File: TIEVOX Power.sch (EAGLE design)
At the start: 15 parts, among them IC1 NE555P, T1 2N222A

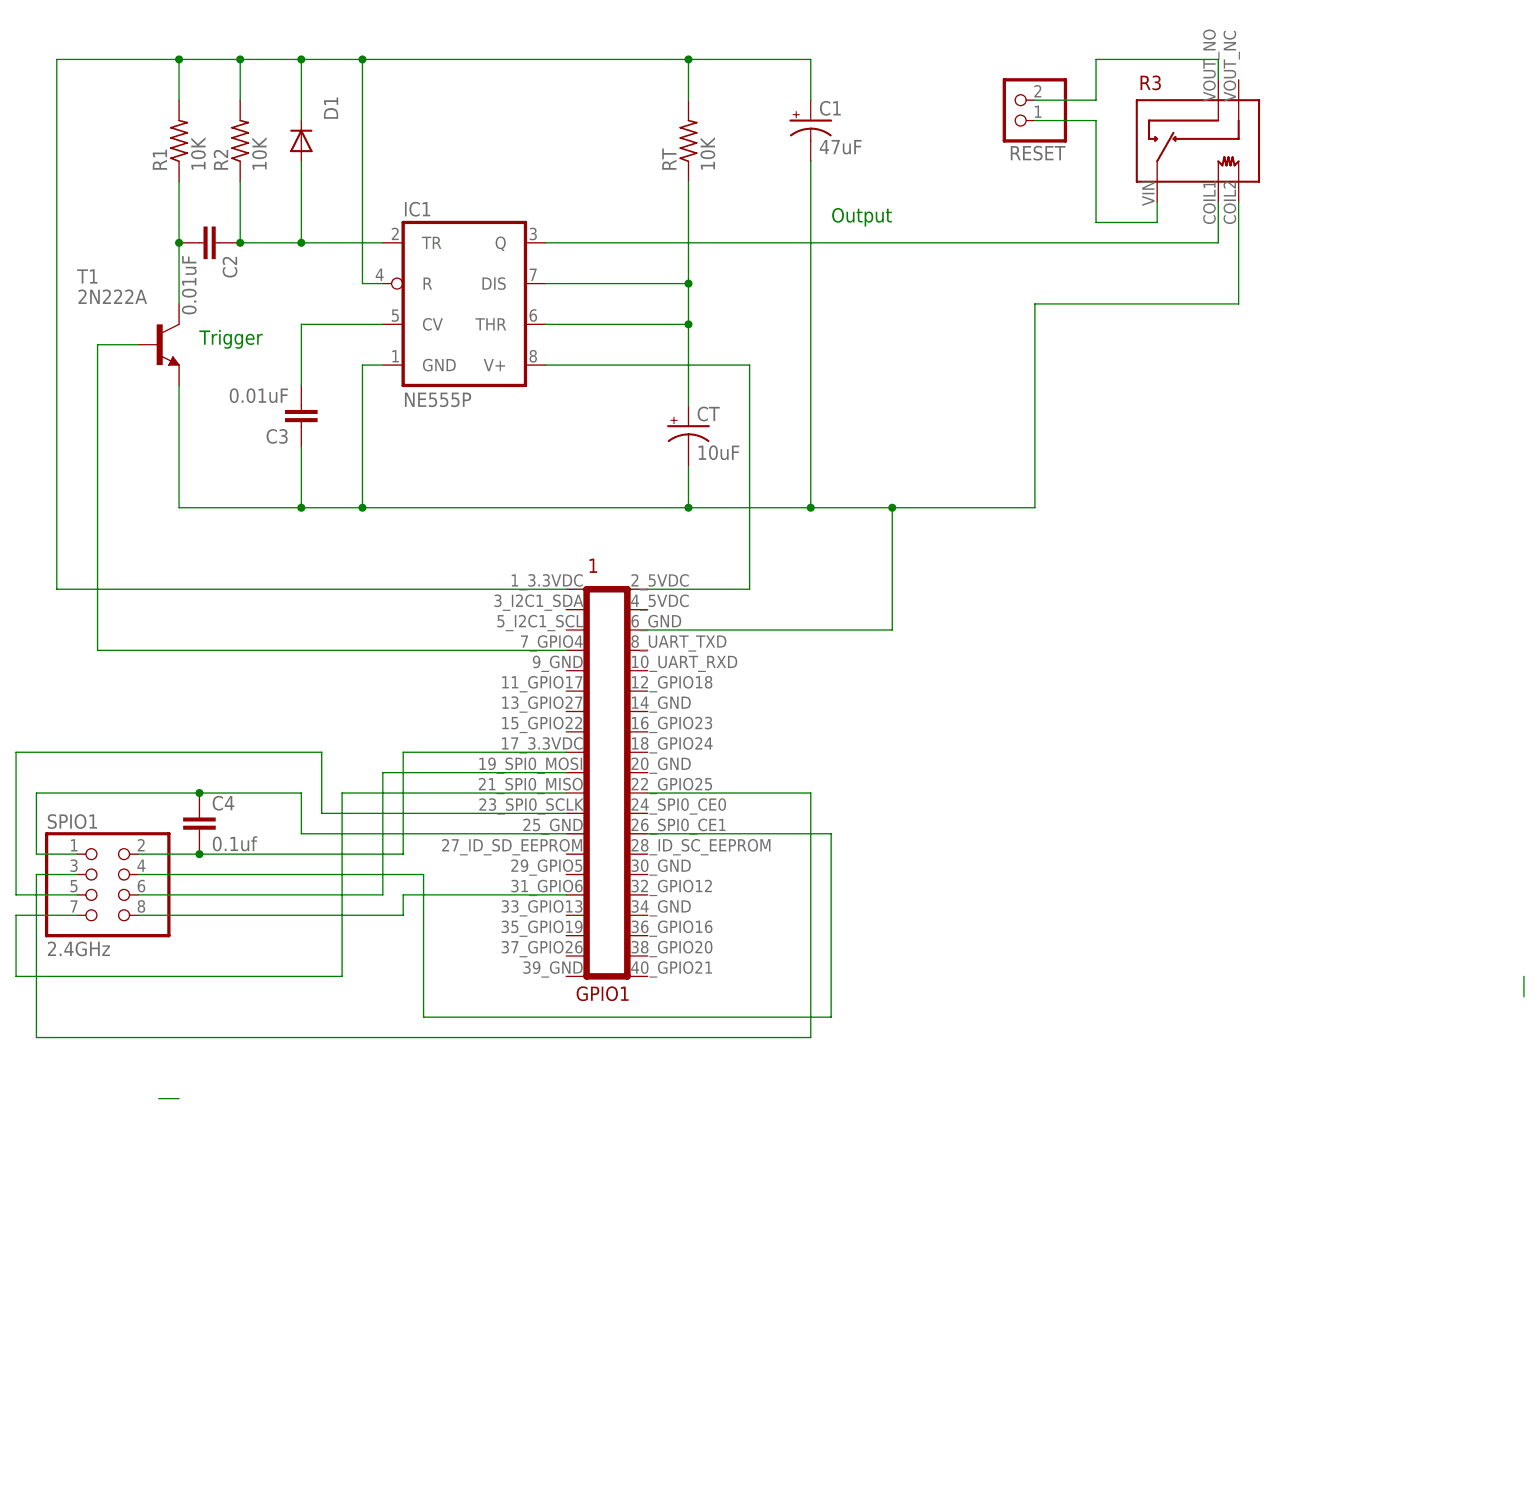
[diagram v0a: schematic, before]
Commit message: Should have working versions of all required boards now.
Updated to No Commercial license.
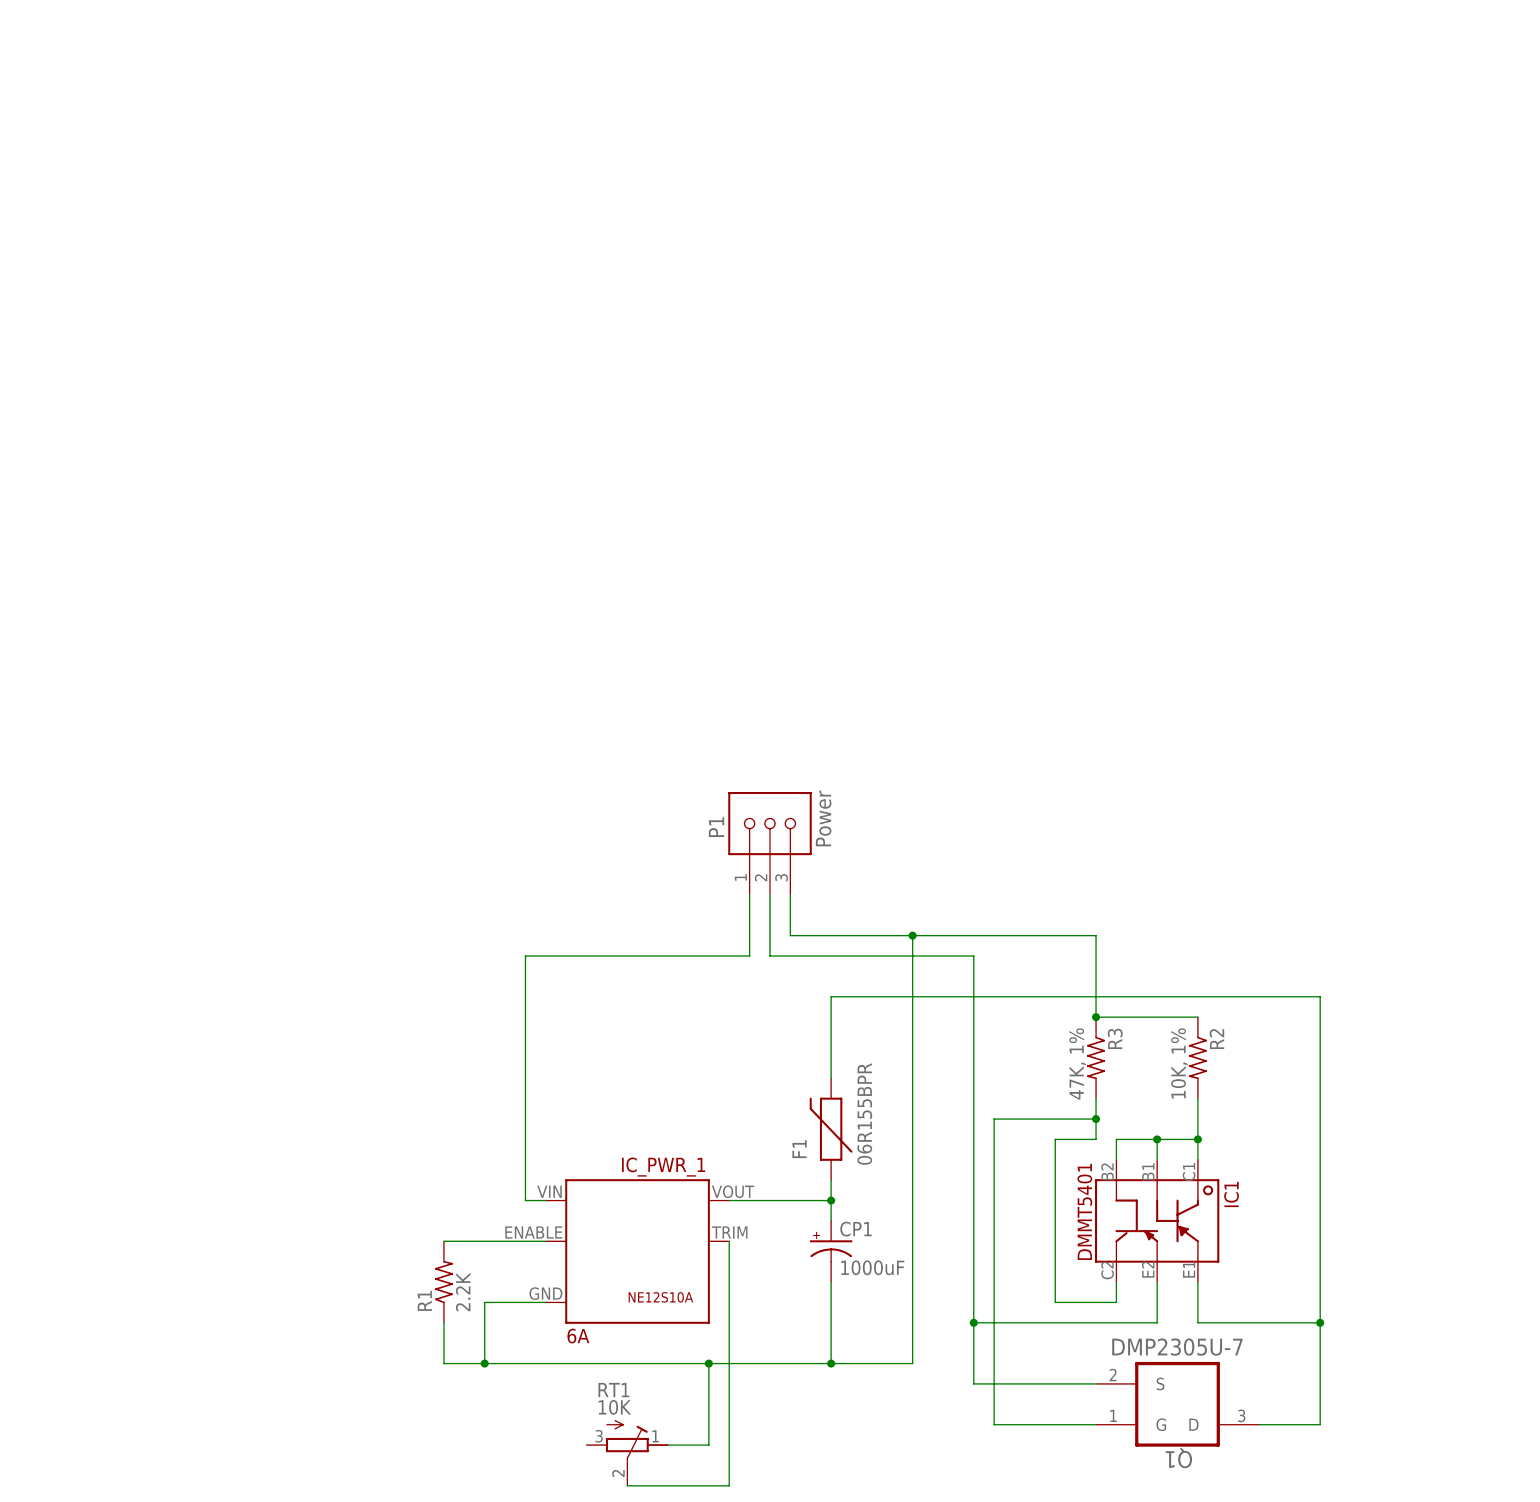
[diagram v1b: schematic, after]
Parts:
- removed C1: 47uF, rcl:CPOL-USE2.5-5
- removed C2, C3: 0.01uF, capacitor-wima:C10/4
- removed C4: 0.1uf, capacitor-wima:C5/2.5
- removed CT: 10uF, rcl:CPOL-USE2.5-5
- removed D1: 1N4148, diode:1N4148DO35-7
- removed GPIO1: RPI_GPIO_MALE_OPEN, connectors:RPI_GPIO_MALE_OPEN
- removed RESET: (no value), pinhead:PINHD-1X2
- removed RT: 10K, resistor:R-US_0207/10
- removed SPIO1: 2.4GHz, pinhead:PINHD-2X4
- removed T1: 2N222A, transistor-neu-to92:2N2222-NPN-TO92-EBC
- added CP1: 1000uF, rcl:CPOL-USE3.5-8
- added F1: 06R155BPR, SparkFun-PowerIC:PTCPTH
- added IC_PWR_1: 6A, packages:NE12S12V6A
- added P1: Power, connector:CONN3-L
- added Q1: DMP2305U-7, Diodes_Inc_By_element14_Batch_1:DMP2305U-7
- added RT1: 10K, resistor:R-TRIMM3006P
- IC1: value NE555P -> DMMT5401; device linear:NE555P -> Diodes_Inc_By_element14_Batch_1:DMMT5401DMMT
- R1: value 10K -> 2.2K; device resistor:R-US_0207/10 -> adafruit:R-US_0207/10
- R2: value 10K -> 10K, 1%; device resistor:R-US_0207/10 -> adafruit:R-US_0207/7
- R3: value 5VDC -> 47K, 1%; device te-connectivity:OUAZ-OUAZ-SS-105D -> adafruit:R-US_0207/7
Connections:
- removed net +3.3VDC: C1.+, D1.C, GPIO1.1_3.3VDC, IC1.R, R1.2, R2.2, RT.2
- removed net N$1: C2.2, R1.1, T1.C
- removed net N$10: C4.2, GPIO1.17_3.3VDC, SPIO1.2
- removed net N$11: GPIO1.26_SPI0_CE1, SPIO1.4
- removed net N$12: GPIO1.19_SPI0_MOSI, SPIO1.6
- removed net N$13: GPIO1.21_SPI0_MISO, SPIO1.7
- removed net N$14: GPIO1.23_SPI0_SCLK, SPIO1.5
- removed net N$15: GPIO1.31_GPIO6, SPIO1.8
- removed net N$2: C2.1, D1.A, IC1.TR, R2.1
- removed net N$3: CT.+, IC1.DIS, IC1.THR, RT.1
- removed net N$4: GPIO1.2_5VDC, IC1.V+
- removed net N$5: C3.2, IC1.CV
- removed net N$6: R3.VIN, RESET.1
- removed net N$7: R3.VOUT_NO, RESET.2
- removed net N$8: GPIO1.7_GPIO4, T1.B
- removed net N$9: C4.1, GPIO1.25_GND, SPIO1.1
- removed net RESET_OUT: IC1.Q, R3.COIL1
- new net +5VDC: IC1.E2, P1.2, Q1.S
- new net GND_PC: CP1.-, IC_PWR_1.GND, P1.3, R1.1, R2.1, R3.1, RT1.E
- new net IN: F1.2, IC1.E1, Q1.D
- new net N$28: CP1.+, F1.1, IC_PWR_1.VOUT
- new net N$29: IC_PWR_1.ENABLE, R1.2
- new net N$32: IC1.B1, IC1.B2, IC1.C1, R2.2
- new net PWR12_TRIM: IC_PWR_1.TRIM, RT1.S
- net GND: now also IC1.C2, Q1.G, R3.2; no longer C1.-, C3.1, CT.-, GPIO1.6_GND, IC1.GND, R3.COIL2, T1.E
- net N$16: now also IC_PWR_1.VIN, P1.1; no longer GPIO1.22_GPIO25, SPIO1.3
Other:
- note added: "Backpower Protection"
- note added: "Power Conversion ~12VDC to 5VDC"
- note removed: "Output"
- note removed: "SPIO 2.4GHz"
- note removed: "Trigger"
- moved on the sheet: R1, R2
